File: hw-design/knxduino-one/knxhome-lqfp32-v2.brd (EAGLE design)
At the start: 38.9 x 38.9 mm, 44 parts, among them IC1 LDL1117S33, IC3 BD9G101, IC4 STM32G071KBT6, P1 B10B-PH-K, P2 B10B-PH-K, P3 B6B-PH-K, U1 OSCILLATOR5X3-PIN1-INDICATED

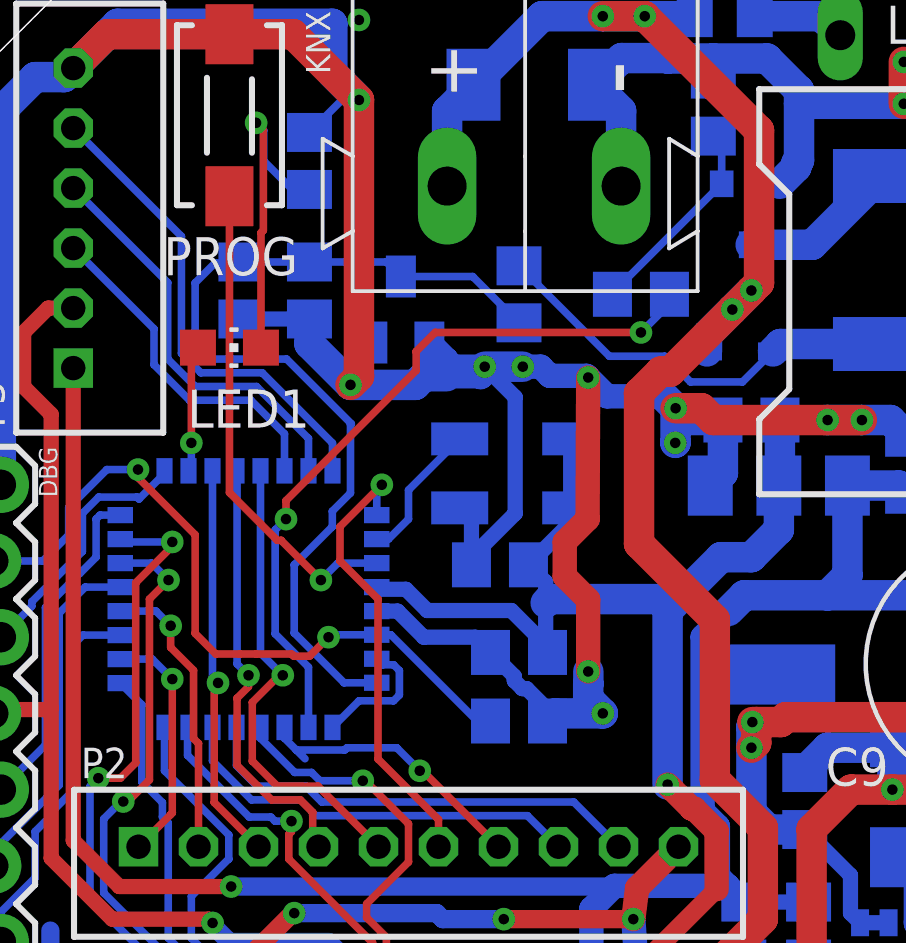
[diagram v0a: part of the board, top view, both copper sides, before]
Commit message: STM32G071 LQFP32 design v1.0
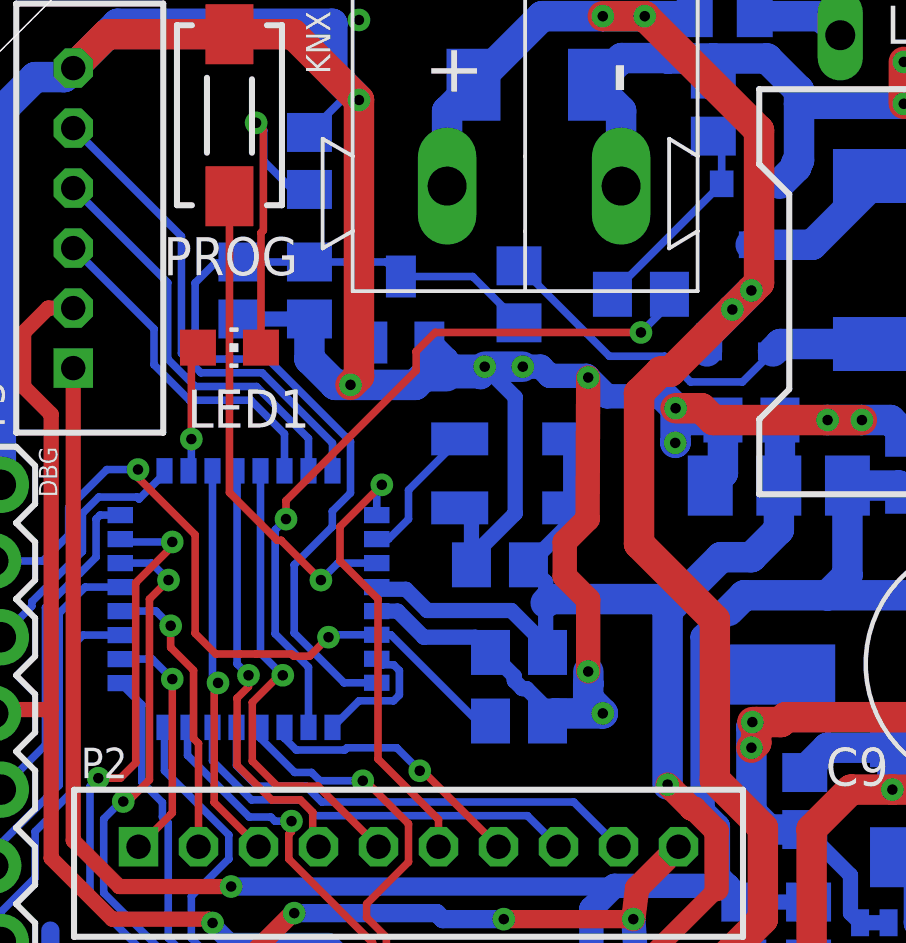
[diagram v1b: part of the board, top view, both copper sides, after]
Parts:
- C12: value 10n -> 100n
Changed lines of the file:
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@@
 <?xml version="1.0" encoding="utf-8"?>
 <!DOCTYPE eagle SYSTEM "eagle.dtd">
-<eagle version="9.3.1">
+<eagle version="9.4.0">
 <drawing>
 <settings>
@@
 <attribute name="VALUE" x="28.448" y="28.321" size="1.27" layer="28" rot="MR90"/>
 </element>
-<element name="C12" library="rcl" library_urn="urn:adsk.eagle:library:334" package="C0805" package3d_urn="urn:adsk.eagle:package:23617/2" value="10n" x="22.987" y="27.813" smashed="yes" rot="MR0">
+<element name="C12" library="rcl" library_urn="urn:adsk.eagle:library:334" package="C0805" package3d_urn="urn:adsk.eagle:package:23617/2" value="100n" x="22.987" y="27.813" smashed="yes" rot="MR0">
 <attribute name="NAME" x="28.067" y="27.051" size="1.27" layer="26" rot="MR0"/>
 <attribute name="SPICEPREFIX" value="C" x="22.987" y="27.813" size="1.778" layer="28" rot="MR0" display="off"/>
@@
 <wire x1="16.51" y1="25.0816" x2="15.7533875" y2="25.0816" width="1.016" layer="16"/>
 <wire x1="15.7533875" y1="25.0816" x2="15.4655875" y2="24.7938" width="1.016" layer="16"/>
-<wire x1="11.938" y1="26.162" x2="11.938" y2="26.99" width="1.016" layer="16"/>
-<wire x1="13.3062" y1="24.7938" x2="11.938" y2="26.162" width="1.016" layer="16"/>
+<wire x1="11.938" y1="25.654" x2="11.938" y2="26.99" width="1.016" layer="16"/>
+<wire x1="13.3062" y1="24.7938" x2="12.7982" y2="24.7938" width="1.016" layer="16"/>
+<wire x1="12.7982" y1="24.7938" x2="11.938" y2="25.654" width="1.016" layer="16"/>
 <via x="13.3062" y="24.7938" extent="1-16" drill="0.35"/>
 <wire x1="15.4655875" y1="24.7938" x2="13.3062" y2="24.7938" width="1.016" layer="16"/>
@@
 <wire x1="17.381" y1="28.405" x2="14.986" y2="28.405" width="0.254" layer="16"/>
 <wire x1="11.938" y1="28.89" x2="9.652" y2="28.89" width="0.254" layer="16"/>
-<wire x1="12.7" y1="20.58344375" x2="13.3062" y2="21.18964375" width="0.254" layer="16"/>
+<wire x1="13.3062" y1="21.18964375" x2="12.7" y2="20.58344375" width="0.254" layer="16"/>
 <wire x1="9.652" y1="28.856975" x2="9.652" y2="28.89" width="0.254" layer="16"/>
 <wire x1="14.986" y1="28.405" x2="14.501" y2="28.89" width="0.254" layer="16"/>
@@
 <wire x1="11.43" y1="16.52416875" x2="13.09116875" y2="14.863" width="0.254" layer="16"/>
 <wire x1="13.09116875" y1="14.863" x2="14.181" y2="14.863" width="0.254" layer="16"/>
-<wire x1="13.3062" y1="23.4662" x2="13.335" y2="23.495" width="0.254" layer="16"/>
-<wire x1="13.335" y1="23.495" x2="11.176" y2="25.654" width="0.254" layer="16"/>
-<wire x1="8.509" y1="25.654" x2="8.128" y2="26.035" width="0.254" layer="16"/>
+<wire x1="8.128" y1="26.035" x2="8.509" y2="25.654" width="0.254" layer="16"/>
 <wire x1="8.128" y1="26.035" x2="8.128" y2="28.194" width="0.254" layer="16"/>
 <wire x1="8.790975" y1="28.856975" x2="9.652" y2="28.856975" width="0.254" layer="16"/>
-<wire x1="13.3062" y1="21.18964375" x2="13.3062" y2="23.4662" width="0.254" layer="16"/>
-<wire x1="11.176" y1="25.654" x2="8.509" y2="25.654" width="0.254" layer="16"/>
 <wire x1="8.128" y1="28.194" x2="8.790975" y2="28.856975" width="0.254" layer="16"/>
+<wire x1="10.55258125" y1="25.654" x2="13.3062" y2="22.90038125" width="0.254" layer="16"/>
+<wire x1="13.3062" y1="22.90038125" x2="13.3062" y2="21.18964375" width="0.254" layer="16"/>
+<wire x1="8.509" y1="25.654" x2="10.55258125" y2="25.654" width="0.254" layer="16"/>
 </signal>
 <signal name="SWCLK">
@@
 <contactref element="T1" pad="3"/>
 <contactref element="R7" pad="2"/>
-<contactref element="C12" pad="2"/>
 <wire x1="25.4" y1="33.086" x2="25.6794" y2="32.8066" width="0.254" layer="16"/>
 <wire x1="25.6794" y1="32.8066" x2="25.6794" y2="31.496" width="0.254" layer="16"/>
-<wire x1="25.6794" y1="31.496" x2="22.037" y2="27.8536" width="0.254" layer="16"/>
-<wire x1="22.037" y1="27.8536" x2="22.037" y2="27.813" width="0.254" layer="16"/>
+<wire x1="22.037" y1="27.8536" x2="25.6794" y2="31.496" width="0.254" layer="16"/>
+<contactref element="C12" pad="2"/>
+<wire x1="22.037" y1="27.813" x2="22.037" y2="27.8536" width="0.254" layer="16"/>
 </signal>
 <signal name="OSC">
@@
 <contactref element="LED1" pad="A"/>
 <wire x1="8.221" y1="26.035" x2="8.001" y2="25.815" width="0.254" layer="1"/>
-<wire x1="8.001" y1="25.815" x2="8.001" y2="22.86" width="0.254" layer="1"/>
-<via x="8.001" y="22.86" extent="1-16" drill="0.35"/>
-<wire x1="8.001" y1="22.86" x2="8.001" y2="22.023" width="0.254" layer="16"/>
+<wire x1="8.001" y1="25.815" x2="8.001" y2="22.987" width="0.254" layer="1"/>
+<via x="8.001" y="22.987" extent="1-16" drill="0.35"/>
+<wire x1="8.001" y1="22.987" x2="8.001" y2="22.023" width="0.254" layer="16"/>
 <wire x1="8.001" y1="22.023" x2="7.906" y2="21.928" width="0.254" layer="16"/>
 </signal>
@@
 <wire x1="11.106" y1="13.378" x2="11.106" y2="13.016025" width="0.254" layer="16"/>
 <wire x1="11.106" y1="13.016025" x2="11.499225" y2="12.6228" width="0.254" layer="16"/>
-<wire x1="11.499225" y1="12.6228" x2="11.7899375" y2="12.3320875" width="0.254" layer="16"/>
 <wire x1="18.161" y1="9.477" x2="18.24" y2="9.398" width="0.254" layer="1"/>
 <wire x1="14.84881875" y1="12.6960125" x2="15.613915625" y2="11.930915625" width="0.254" layer="16"/>
